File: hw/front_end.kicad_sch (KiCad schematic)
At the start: 6 parts, among them Q4 SSM6P35AFE, Q5 SSM6P35AFE

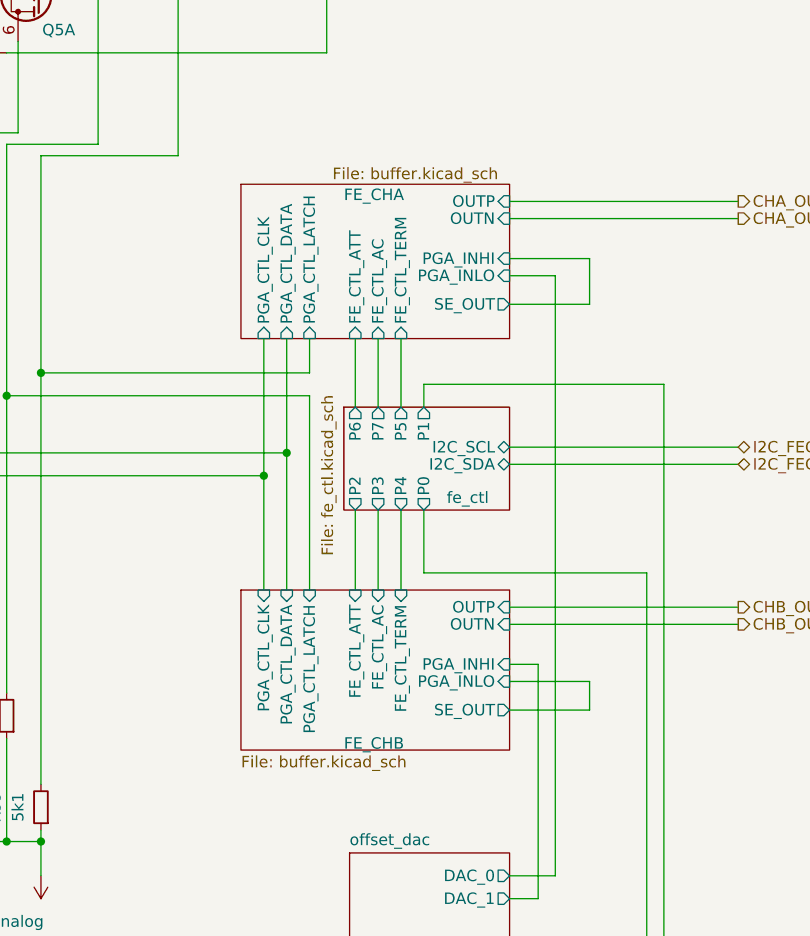
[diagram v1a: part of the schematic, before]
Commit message: removed buffer and 100n DAC output caps
 - prep for updating PCB to remove buffer stuff
 - caps were moved to buffer (close to switch)
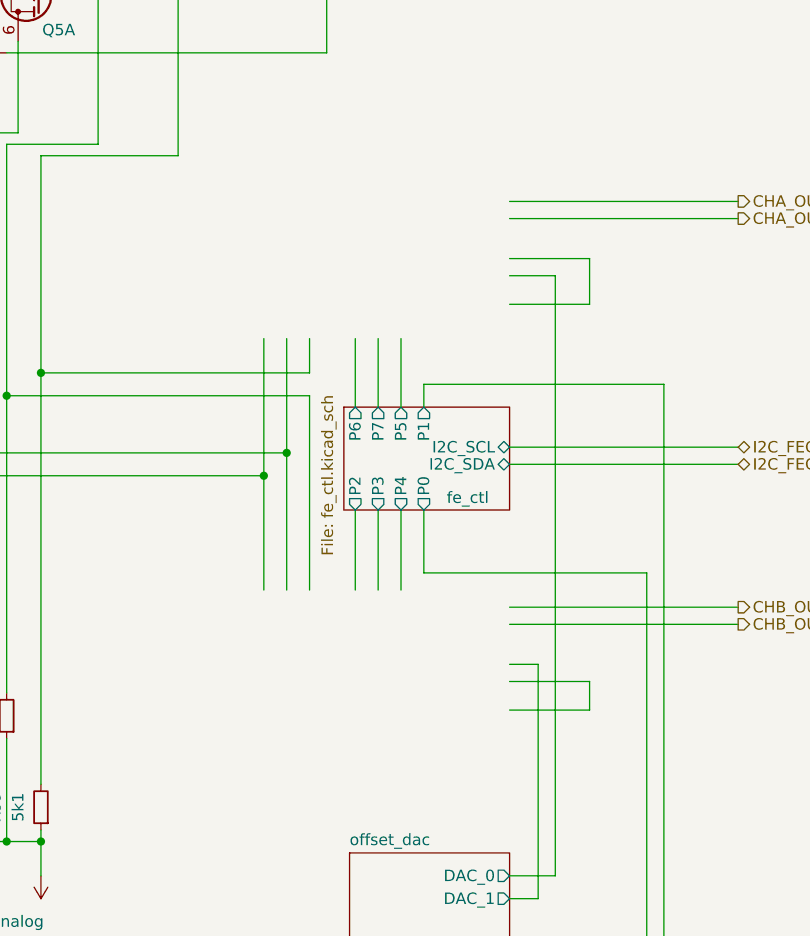
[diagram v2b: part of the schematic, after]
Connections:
- net FE_CHA/PGA_CTL_CLK: no longer names the net of Q4.3 (D), R96.2
- net FE_CHA/PGA_CTL_DATA: no longer names the net of Q5.6 (D), R97.2
- net FE_CHA/PGA_CTL_LATCH: no longer names the net of Q4.6 (D), R99.2
- net FE_CHB/PGA_CTL_LATCH: no longer names the net of Q5.3 (D), R98.2
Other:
- removed sheet FE_CHA
- removed sheet FE_CHB

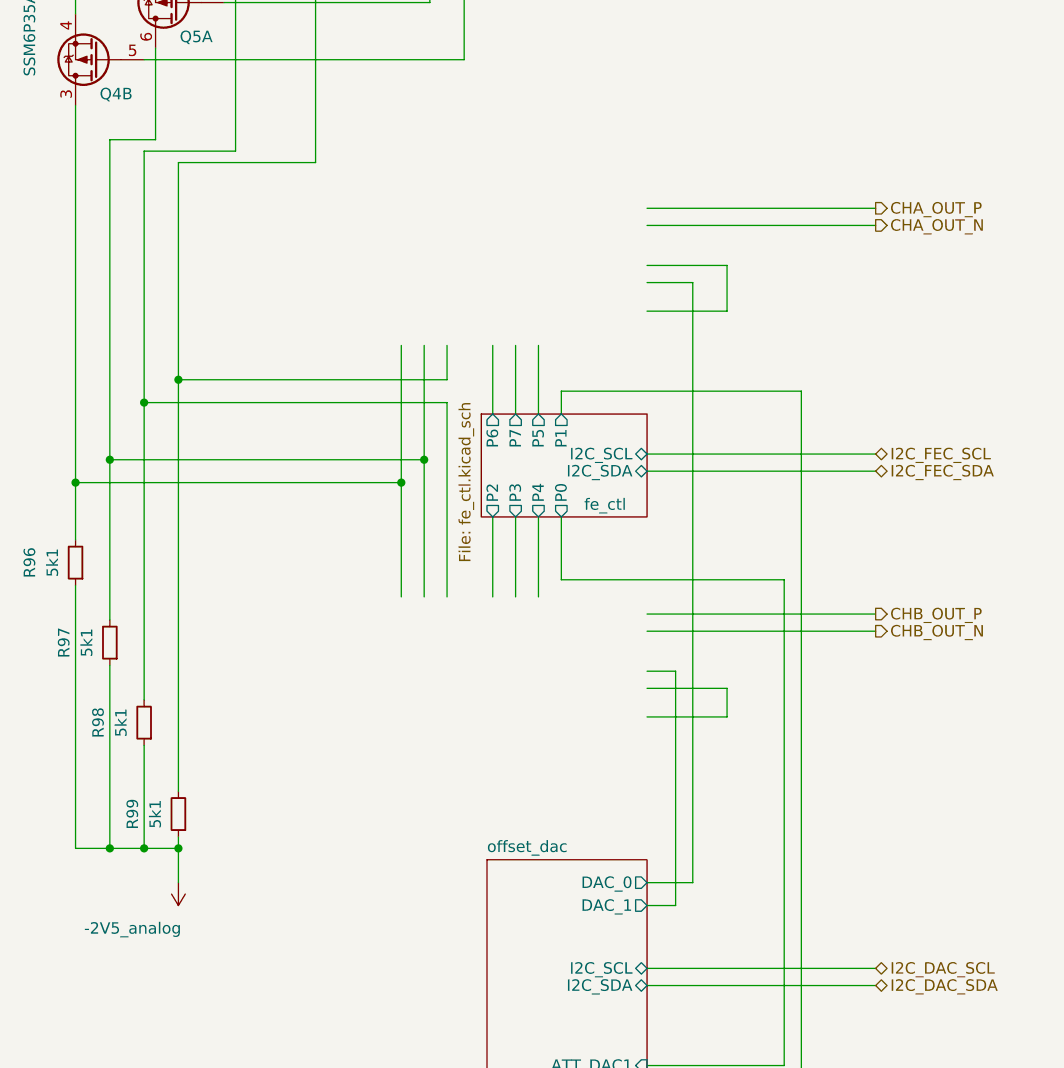
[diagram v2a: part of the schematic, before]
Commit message: sch: re-added buffer to top-project schematic
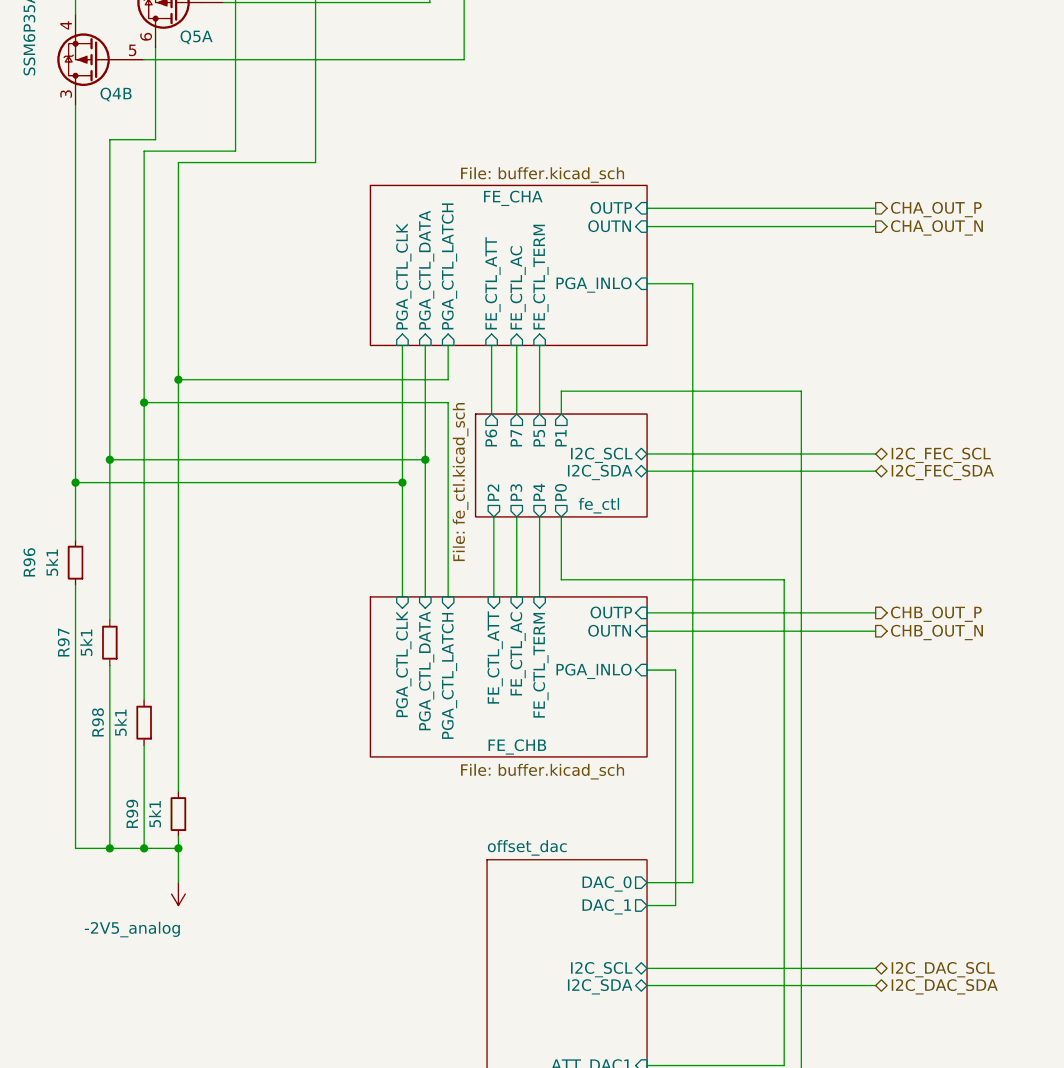
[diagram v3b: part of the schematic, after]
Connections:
- net FE_CHA/PGA_CTL_LATCH: now reaches Q4.6 (D), R99.2
- net FE_CHA/PGA_CTL_CLK: now reaches Q4.3 (D), R96.2
- net FE_CHB/PGA_CTL_LATCH: now reaches Q5.3 (D), R98.2
- net FE_CHA/PGA_CTL_DATA: now reaches Q5.6 (D), R97.2
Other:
- added sheet FE_CHA (buffer.kicad_sch)
- added sheet FE_CHB (buffer.kicad_sch)

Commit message: updated parts assignments
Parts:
- R96, R97, R98, R99: Manufacturer (none) -> Stackpole; Part (none) -> RMCF0603FT5K10
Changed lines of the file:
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@@
 			)
 		)
-		(property "Part" ""
+		(property "Part" "RMCF0603FT5K10"
 			(at 71.12 146.05 90)
 			(effects
@@
 			)
 		)
-		(property "Manufacturer" ""
+		(property "Manufacturer" "Stackpole"
 			(at 71.12 146.05 90)
 			(effects
@@
 			)
 		)
-		(property "Part" ""
+		(property "Part" "RMCF0603FT5K10"
 			(at 59.69 118.11 90)
 			(effects
@@
 			)
 		)
-		(property "Manufacturer" ""
+		(property "Manufacturer" "Stackpole"
 			(at 59.69 118.11 90)
 			(effects
@@
 			)
 		)
-		(property "Part" ""
+		(property "Part" "RMCF0603FT5K10"
 			(at 67.31 135.89 90)
 			(effects
@@
 			)
 		)
-		(property "Manufacturer" ""
+		(property "Manufacturer" "Stackpole"
 			(at 67.31 135.89 90)
 			(effects
@@
 			)
 		)
-		(property "Part" ""
+		(property "Part" "RMCF0603FT5K10"
 			(at 63.5 127 90)
 			(effects
@@
 			)
 		)
-		(property "Manufacturer" ""
+		(property "Manufacturer" "Stackpole"
 			(at 63.5 127 90)
 			(effects

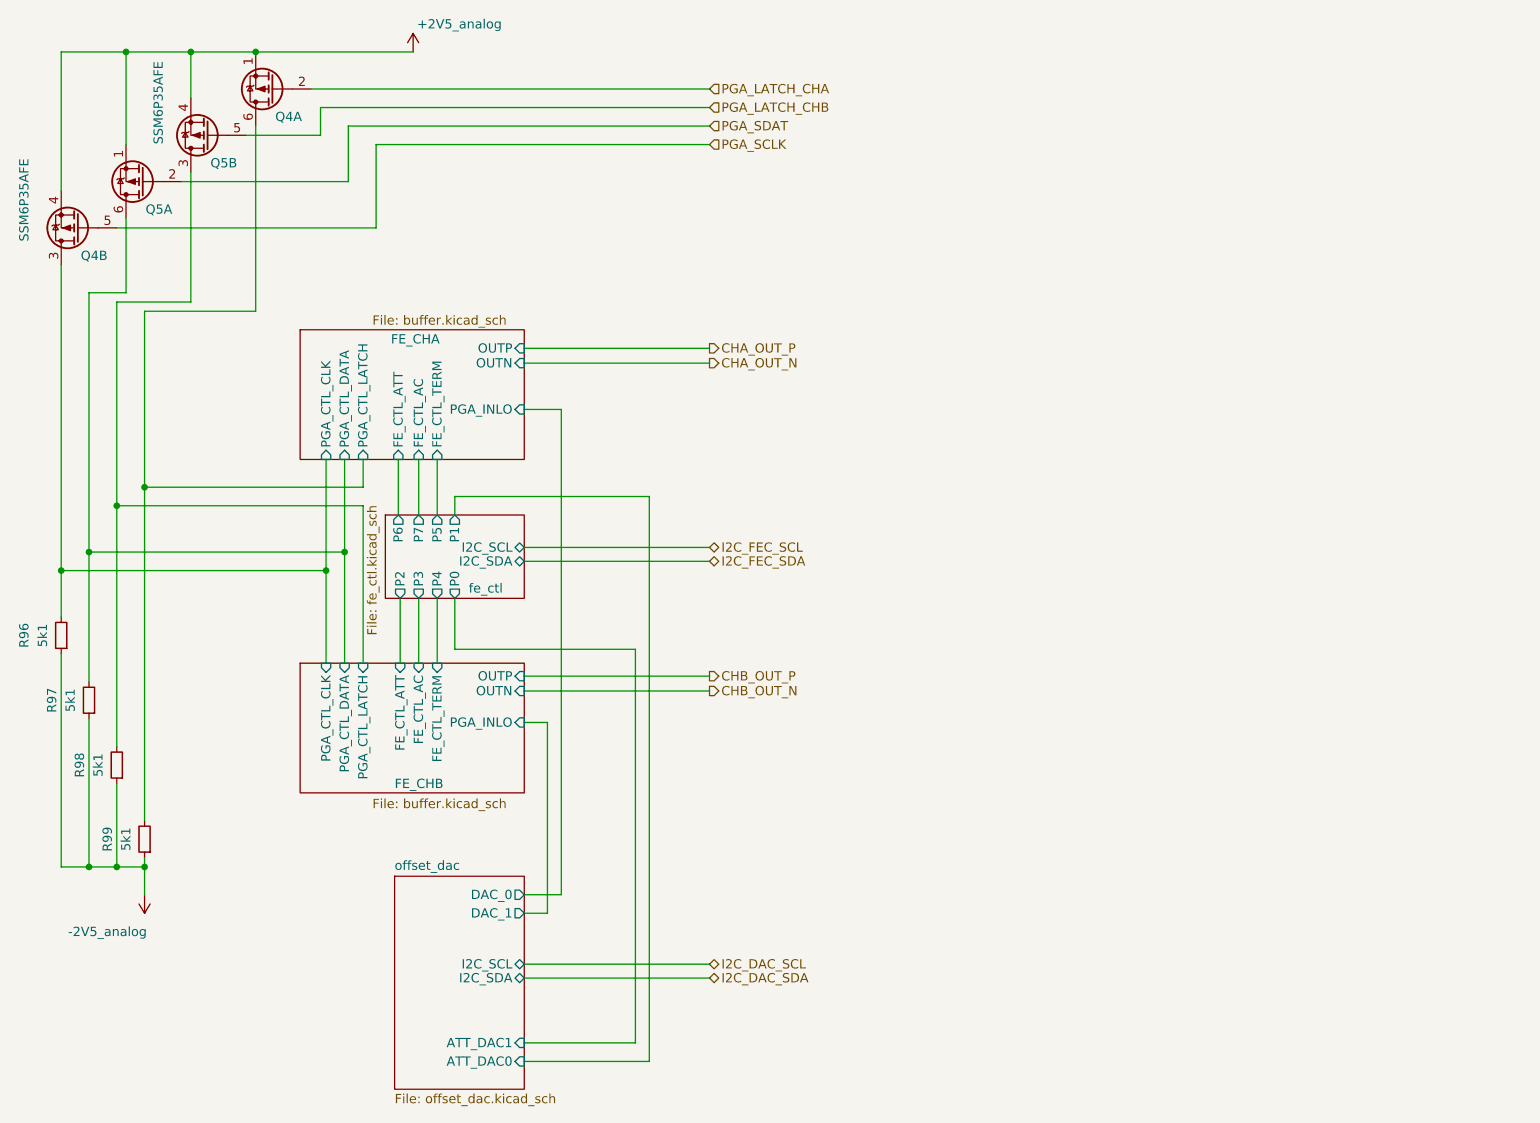
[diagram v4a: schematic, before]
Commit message: fixed BOM; added relay drivers
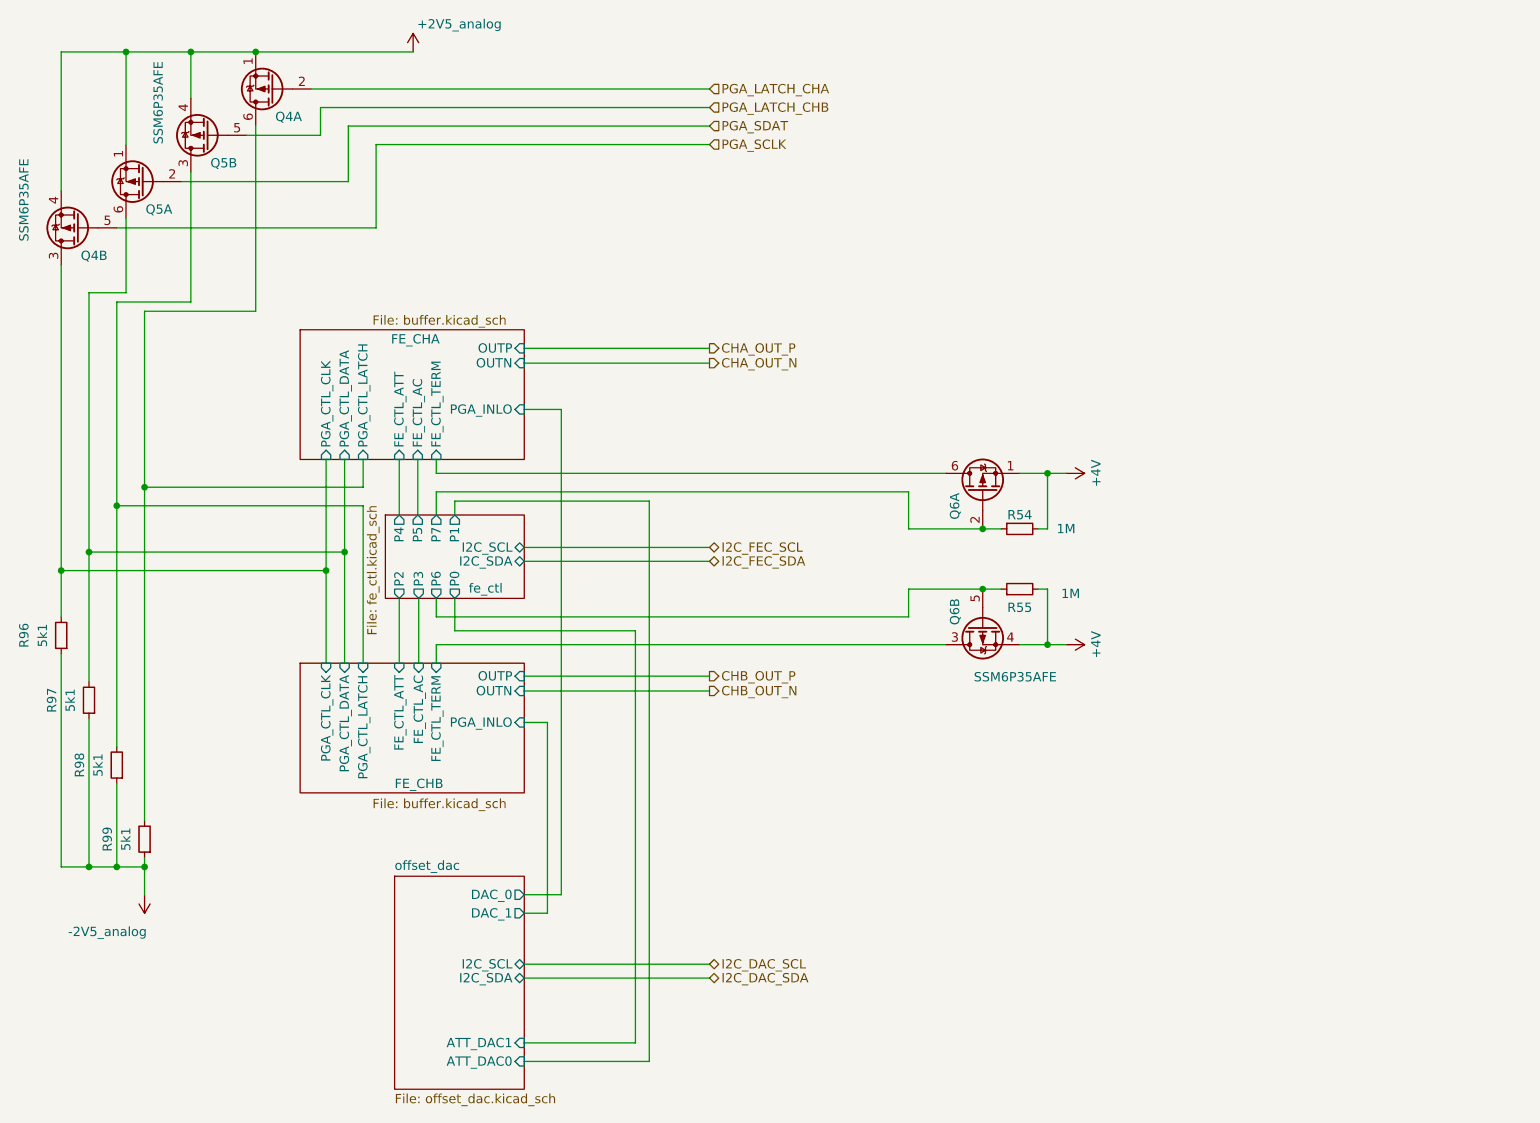
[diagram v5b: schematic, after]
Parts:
- added Q6: SSM6P35AFE, proj_footprints:SOT-563-adjusted, symbol Device:Q_Dual_PMOS_S1G1D2S2G2D1
- added R54, R55: 1M, Resistor_SMD:R_0603_1608Metric, symbol Device:R_Small
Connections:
- net FE_CHA/FE_CTL_TERM: now also Q6.6 (D)
- net FE_CHB/FE_CTL_TERM: now also Q6.3 (D)
- new net +4V: Q6.1 (S), Q6.4 (S), R54.2, R55.2
- new net fe_ctl/P6: Q6.5 (G), R55.1
- new net fe_ctl/P7: Q6.2 (G), R54.1

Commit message: connected versaclock CLKSEL to ULPI RSTB (share FPGA pin)
ULPI Rstb is unlikely to be used

Also: - update of kicad to 9.0 (many library footprints updated)
      - added sheet titles, author
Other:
- company: (none) -> Till Straumann
- title: (none) -> Front End
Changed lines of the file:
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@@
 (kicad_sch
-	(version 20231120)
+	(version 20250114)
 	(generator "eeschema")
-	(generator_version "8.0")
+	(generator_version "9.0")
 	(paper "A4")
+	(title_block
+		(title "Front End")
+		(rev "3.3b")
+		(company "Till Straumann")
+	)
 	(junction
 		(at 98.552 106.68)
@@
 		(at 105.41 151.13)
 		(size 17.78 29.21)
+		(exclude_from_sim no)
+		(in_bom yes)
+		(on_board yes)
+		(dnp no)
 		(fields_autoplaced yes)
 		(stroke
@@
 		(at 92.456 121.92)
 		(size 30.734 17.78)
+		(exclude_from_sim no)
+		(in_bom yes)
+		(on_board yes)
+		(dnp no)
 		(stroke
 			(width 0.1524)
@@
 		(at 104.14 101.6)
 		(size 19.05 11.43)
+		(exclude_from_sim no)
+		(in_bom yes)
+		(on_board yes)
+		(dnp no)
 		(stroke
 			(width 0.1524)
@@
 		(at 92.456 76.2)
 		(size 30.734 17.78)
+		(exclude_from_sim no)
+		(in_bom yes)
+		(on_board yes)
+		(dnp no)
 		(stroke
 			(width 0.1524)

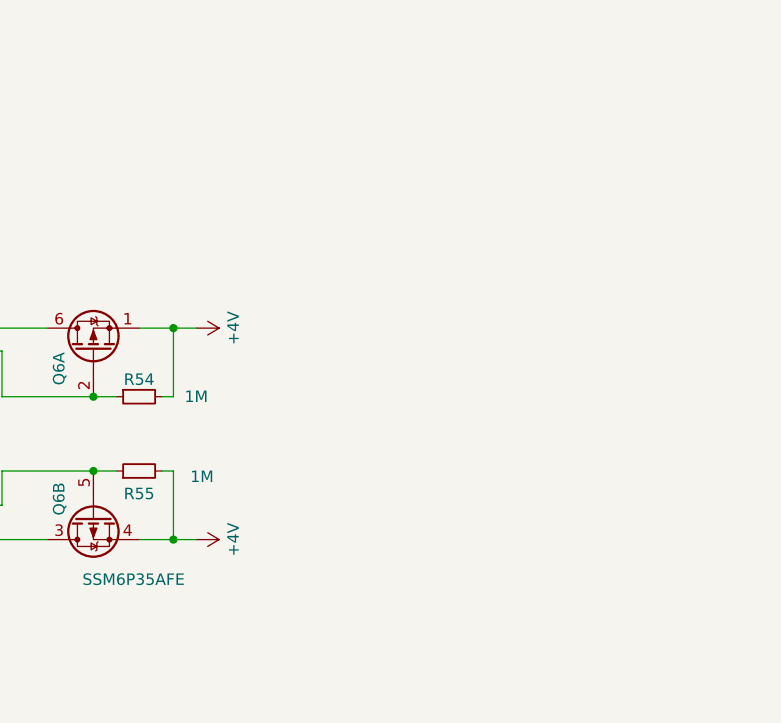
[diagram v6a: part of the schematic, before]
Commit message: added 3V relay option (different 0ohm jumpers)
Also: another kicad updat
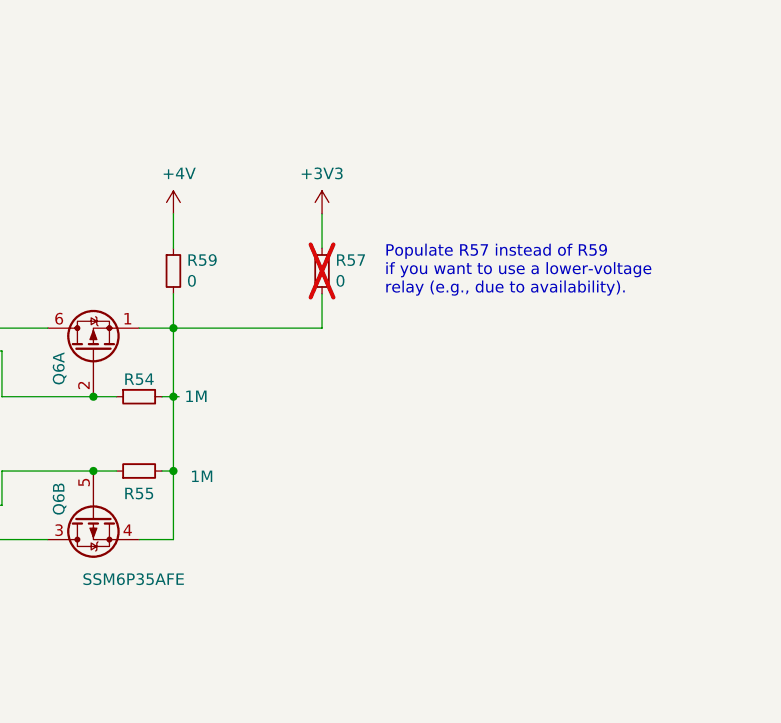
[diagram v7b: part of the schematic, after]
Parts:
- added R57, R59: 0, Resistor_SMD:R_0603_1608Metric, symbol Device:R_Small
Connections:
- net +4V: now also R59.1; no longer Q6.1 (S), Q6.4 (S), R54.2, R55.2
- new net: Q6.1 (S), Q6.4 (S), R54.2, R55.2, R57.2, R59.2
- new net +3V3: R57.1
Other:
- note added: "Populate R57 instead of R59 if you want to use a lower-voltage relay (e.g., due to availability)."

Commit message: Added licensing information
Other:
- company: Till Straumann -> Copyright Till Straumann, 2025
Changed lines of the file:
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@@
 		(title "Front End")
 		(rev "3.3b")
-		(company "Till Straumann")
+		(company "Copyright Till Straumann, 2025")
+		(comment 1 "License: CERN-OHL-P v2")
 	)
 	(text "Populate R57 instead of R59\nif you want to use a lower-voltage\nrelay (e.g., due to availability)."
